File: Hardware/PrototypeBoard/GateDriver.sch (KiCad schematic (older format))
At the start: 38 parts, among them U4 TLE7185-1E

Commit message: more layout and some changes to schematic
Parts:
- TP10, TP11, TP12, TP13, TP14, TP15, TP16, TP17, TP18, TP19, TP20, TP21, TP6, TP7, TP8, TP9: footprint Measurement_Points:Measurement_Point_Round-SMD-Pad_Small -> Pin_Headers:Pin_Header_Straight_1x01_Pitch2.00mm
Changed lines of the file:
@@
 F 0 "TP17" H 6950 2900 50  0000 C BNN
 F 1 "BstV" H 6950 2850 50  0000 C CNN
-F 2 "Measurement_Points:Measurement_Point_Round-SMD-Pad_Small" H 6950 2600 50  0001 C CNN
+F 2 "Pin_Headers:Pin_Header_Straight_1x01_Pitch2.00mm" H 6950 2600 50  0001 C CNN
 F 3 "" H 6950 2600 50  0001 C CNN
 	1    6950 2600
@@
 F 0 "TP16" H 6950 2200 50  0000 C BNN
 F 1 "BstU" H 6950 2150 50  0000 C CNN
-F 2 "Measurement_Points:Measurement_Point_Round-SMD-Pad_Small" H 6950 1900 50  0001 C CNN
+F 2 "Pin_Headers:Pin_Header_Straight_1x01_Pitch2.00mm" H 6950 1900 50  0001 C CNN
 F 3 "" H 6950 1900 50  0001 C CNN
 	1    6950 1900
@@
 F 0 "TP18" H 6950 3600 50  0000 C BNN
 F 1 "BstW" H 6950 3550 50  0000 C CNN
-F 2 "Measurement_Points:Measurement_Point_Round-SMD-Pad_Small" H 6950 3300 50  0001 C CNN
+F 2 "Pin_Headers:Pin_Header_Straight_1x01_Pitch2.00mm" H 6950 3300 50  0001 C CNN
 F 3 "" H 6950 3300 50  0001 C CNN
 	1    6950 3300
@@
 F 0 "TP14" H 6200 3000 50  0000 C BNN
 F 1 "GateVH" H 6200 2950 50  0000 C CNN
-F 2 "Measurement_Points:Measurement_Point_Round-SMD-Pad_Small" H 6200 2700 50  0001 C CNN
+F 2 "Pin_Headers:Pin_Header_Straight_1x01_Pitch2.00mm" H 6200 2700 50  0001 C CNN
 F 3 "" H 6200 2700 50  0001 C CNN
 	1    6200 2700
@@
 F 0 "TP13" H 6200 2300 50  0000 C BNN
 F 1 "GateUH" H 6200 2250 50  0000 C CNN
-F 2 "Measurement_Points:Measurement_Point_Round-SMD-Pad_Small" H 6200 2000 50  0001 C CNN
+F 2 "Pin_Headers:Pin_Header_Straight_1x01_Pitch2.00mm" H 6200 2000 50  0001 C CNN
 F 3 "" H 6200 2000 50  0001 C CNN
 	1    6200 2000
@@
 F 0 "TP15" H 6200 3700 50  0000 C BNN
 F 1 "GateWH" H 6200 3650 50  0000 C CNN
-F 2 "Measurement_Points:Measurement_Point_Round-SMD-Pad_Small" H 6200 3400 50  0001 C CNN
+F 2 "Pin_Headers:Pin_Header_Straight_1x01_Pitch2.00mm" H 6200 3400 50  0001 C CNN
 F 3 "" H 6200 3400 50  0001 C CNN
 	1    6200 3400
@@
 F 0 "TP19" H 6950 4300 50  0000 C BNN
 F 1 "GateUL" H 6950 4250 50  0000 C CNN
-F 2 "Measurement_Points:Measurement_Point_Round-SMD-Pad_Small" H 6950 4000 50  0001 C CNN
+F 2 "Pin_Headers:Pin_Header_Straight_1x01_Pitch2.00mm" H 6950 4000 50  0001 C CNN
 F 3 "" H 6950 4000 50  0001 C CNN
 	1    6950 4000
@@
 F 0 "TP20" H 6950 4800 50  0000 C BNN
 F 1 "GateVL" H 6950 4750 50  0000 C CNN
-F 2 "Measurement_Points:Measurement_Point_Round-SMD-Pad_Small" H 6950 4500 50  0001 C CNN
+F 2 "Pin_Headers:Pin_Header_Straight_1x01_Pitch2.00mm" H 6950 4500 50  0001 C CNN
 F 3 "" H 6950 4500 50  0001 C CNN
 	1    6950 4500
@@
 F 0 "TP21" H 6950 5300 50  0000 C BNN
 F 1 "GateWL" H 6950 5250 50  0000 C CNN
-F 2 "Measurement_Points:Measurement_Point_Round-SMD-Pad_Small" H 6950 5000 50  0001 C CNN
+F 2 "Pin_Headers:Pin_Header_Straight_1x01_Pitch2.00mm" H 6950 5000 50  0001 C CNN
 F 3 "" H 6950 5000 50  0001 C CNN
 	1    6950 5000
@@
 F 0 "TP9" H 1900 3400 50  0000 C BNN
 F 1 "GdEna" H 1900 3350 50  0000 C CNN
-F 2 "Measurement_Points:Measurement_Point_Round-SMD-Pad_Small" H 1900 3100 50  0001 C CNN
+F 2 "Pin_Headers:Pin_Header_Straight_1x01_Pitch2.00mm" H 1900 3100 50  0001 C CNN
 F 3 "" H 1900 3100 50  0001 C CNN
 	1    1900 3100
@@
 F 0 "TP10" H 1900 3700 50  0000 C BNN
 F 1 "PwmUL" H 1900 3650 50  0000 C CNN
-F 2 "Measurement_Points:Measurement_Point_Round-SMD-Pad_Small" H 1900 3400 50  0001 C CNN
+F 2 "Pin_Headers:Pin_Header_Straight_1x01_Pitch2.00mm" H 1900 3400 50  0001 C CNN
 F 3 "" H 1900 3400 50  0001 C CNN
 	1    1900 3400
@@
 F 0 "TP6" H 1700 3900 50  0000 C BNN
 F 1 "~PwmUH" H 1700 3850 50  0000 C CNN
-F 2 "Measurement_Points:Measurement_Point_Round-SMD-Pad_Small" H 1700 3600 50  0001 C CNN
+F 2 "Pin_Headers:Pin_Header_Straight_1x01_Pitch2.00mm" H 1700 3600 50  0001 C CNN
 F 3 "" H 1700 3600 50  0001 C CNN
 	1    1700 3600
@@
 F 0 "TP11" H 1900 4200 50  0000 C BNN
 F 1 "PwmVL" H 1900 4150 50  0000 C CNN
-F 2 "Measurement_Points:Measurement_Point_Round-SMD-Pad_Small" H 1900 3900 50  0001 C CNN
+F 2 "Pin_Headers:Pin_Header_Straight_1x01_Pitch2.00mm" H 1900 3900 50  0001 C CNN
 F 3 "" H 1900 3900 50  0001 C CNN
 	1    1900 3900
@@
 F 0 "TP7" H 1700 4400 50  0000 C BNN
 F 1 "~PwmVH" H 1700 4350 50  0000 C CNN
-F 2 "Measurement_Points:Measurement_Point_Round-SMD-Pad_Small" H 1700 4100 50  0001 C CNN
+F 2 "Pin_Headers:Pin_Header_Straight_1x01_Pitch2.00mm" H 1700 4100 50  0001 C CNN
 F 3 "" H 1700 4100 50  0001 C CNN
 	1    1700 4100
@@
 F 0 "TP12" H 1900 4700 50  0000 C BNN
 F 1 "PwmWL" H 1900 4650 50  0000 C CNN
-F 2 "Measurement_Points:Measurement_Point_Round-SMD-Pad_Small" H 1900 4400 50  0001 C CNN
+F 2 "Pin_Headers:Pin_Header_Straight_1x01_Pitch2.00mm" H 1900 4400 50  0001 C CNN
 F 3 "" H 1900 4400 50  0001 C CNN
 	1    1900 4400
@@
 F 0 "TP8" H 1700 4900 50  0000 C BNN
 F 1 "~PwmWH" H 1700 4850 50  0000 C CNN
-F 2 "Measurement_Points:Measurement_Point_Round-SMD-Pad_Small" H 1700 4600 50  0001 C CNN
+F 2 "Pin_Headers:Pin_Header_Straight_1x01_Pitch2.00mm" H 1700 4600 50  0001 C CNN
 F 3 "" H 1700 4600 50  0001 C CNN
 	1    1700 4600

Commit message: Migrated to kicad 5
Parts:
- C21, C22, C23, C24, C25, C26: symbol C -> Device:C
- R11, R12, R13, R14, R15, R16, R17, R18, R19, R20, R21, R22, R23, R24, R25: symbol R -> Device:R
- TP10, TP11, TP12, TP13, TP14, TP15, TP16, TP17, TP18, TP19, TP20, TP21, TP6, TP7, TP8, TP9: symbol TEST -> PrototypeBoard-rescue:TEST
- U4: symbol TLE7185-1E -> PrototypeBoard-rescue:TLE7185-1E
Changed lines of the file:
@@
-EESchema Schematic File Version 2
-LIBS:power
-LIBS:device
-LIBS:switches
-LIBS:relays
-LIBS:motors
-LIBS:transistors
-LIBS:conn
-LIBS:linear
-LIBS:regul
-LIBS:74xx
-LIBS:cmos4000
-LIBS:adc-dac
-LIBS:memory
-LIBS:xilinx
-LIBS:microcontrollers
-LIBS:dsp
-LIBS:microchip
-LIBS:analog_switches
-LIBS:motorola
-LIBS:texas
-LIBS:intel
-LIBS:audio
-LIBS:interface
-LIBS:digital-audio
-LIBS:philips
-LIBS:display
-LIBS:cypress
-LIBS:siliconi
-LIBS:opto
-LIBS:atmel
-LIBS:contrib
-LIBS:valves
+EESchema Schematic File Version 4
 LIBS:PrototypeBoard-cache
-EELAYER 25 0
+EELAYER 26 0
 EELAYER END
 $Descr A4 11693 8268
@@
 $EndDescr
 $Comp
-L TLE7185-1E U4
+L PrototypeBoard-rescue:TLE7185-1E U4
 U 1 1 56C10CBD
 P 4500 3600
@@
 Logic_GD_ENA
 $Comp
-L R R14
+L Device:R R14
 U 1 1 56C25790
 P 3050 2800
@@
 $EndComp
 $Comp
-L R R13
+L Device:R R13
 U 1 1 56C257FB
 P 3050 2600
@@
 ~Logic_GD_ERR2
 $Comp
-L C C22
+L Device:C C22
 U 1 1 56C25879
 P 2950 2200
@@
 	3150 2350 2950 2350
 $Comp
-L C C21
+L Device:C C21
 U 1 1 56C25915
 P 2600 2050
@@
 	2600 1900 3300 1900
 $Comp
-L GND #PWR032
+L power:GND #PWR032
 U 1 1 56C259AC
 P 2600 2200
@@
 $EndComp
 $Comp
-L R R11
+L Device:R R11
 U 1 1 56C25A1A
 P 1800 4950
@@
 $EndComp
 $Comp
-L R R12
+L Device:R R12
 U 1 1 56C25AD5
 P 1800 5250
@@
 $EndComp
 $Comp
-L R R15
+L Device:R R15
 U 1 1 56C25B0C
 P 3100 5450
@@
 	3300 5300 3100 5300
 $Comp
-L GND #PWR033
+L power:GND #PWR033
 U 1 1 56C25C22
 P 1800 5400
@@
 $EndComp
 $Comp
-L GND #PWR034
+L power:GND #PWR034
 U 1 1 56C25CA5
 P 3100 5600
@@
 $EndComp
 $Comp
-L +3.3V #PWR035
+L power:+3.3V #PWR035
 U 1 1 56C25D62
 P 1800 4800
@@
 $EndComp
 $Comp
-L R R18
+L Device:R R18
 U 1 1 56C25E1E
 P 4500 1050
@@
 $EndComp
 $Comp
-L C C23
+L Device:C C23
 U 1 1 56C25EA2
 P 4700 1450
@@
 $EndComp
 $Comp
-L GND #PWR036
+L power:GND #PWR036
 U 1 1 56C2602E
 P 4700 1600
@@
 $EndComp
 $Comp
-L +BATT #PWR037
+L power:+BATT #PWR037
 U 1 1 56C261FD
 P 4500 800
@@
 $EndComp
 $Comp
-L R R19
+L Device:R R19
 U 1 1 56C26356
 P 4950 1350
@@
 	4950 1500 4950 1600
 $Comp
-L +BATT #PWR038
+L power:+BATT #PWR038
 U 1 1 56C26408
 P 4950 1200
@@
 Source_W_H
 $Comp
-L C C24
+L Device:C C24
 U 1 1 56C26607
 P 6950 2100
@@
 $EndComp
 $Comp
-L C C25
+L Device:C C25
 U 1 1 56C266D2
 P 6950 2800
@@
 $EndComp
 $Comp
-L C C26
+L Device:C C26
 U 1 1 56C26727
 P 6950 3500
@@
 Gate_W_L
 $Comp
-L R R25
+L Device:R R25
 U 1 1 56C2703F
 P 5950 5100
@@
 $EndComp
 $Comp
-L R R24
+L Device:R R24
 U 1 1 56C271C9
 P 5950 4600
@@
 Gate_U_L
 $Comp
-L R R23
+L Device:R R23
 U 1 1 56C27221
 P 5950 4100
@@
 $EndComp
 $Comp
-L R R22
+L Device:R R22
 U 1 1 56C2752F
 P 5950 3500
@@
 $EndComp
 $Comp
-L R R21
+L Device:R R21
 U 1 1 56C2759F
 P 5950 2800
@@
 $EndComp
 $Comp
-L R R20
+L Device:R R20
 U 1 1 56C27617
 P 5950 2100
@@
 $EndComp
 $Comp
-L GND #PWR039
+L power:GND #PWR039
 U 1 1 56C35C82
 P 4050 5600
@@
 $EndComp
 $Comp
-L GND #PWR040
+L power:GND #PWR040
 U 1 1 56C35CC9
 P 4350 5600
@@
 $EndComp
 $Comp
-L GND #PWR041
+L power:GND #PWR041
 U 1 1 56C35D10
 P 4650 5600
@@
 $EndComp
 $Comp
-L GND #PWR042
+L power:GND #PWR042
 U 1 1 56C35D57
 P 4950 5600
@@
 $EndComp
 $Comp
-L R R16
+L Device:R R16
 U 1 1 56C36A2B
 P 3850 1450
@@
 $EndComp
 $Comp
-L GND #PWR043
+L power:GND #PWR043
 U 1 1 56C36B52
 P 3850 1600
@@
 $EndComp
 $Comp
-L R R17
+L Device:R R17
 U 1 1 56C36CC4
 P 4050 1050
@@
 $EndComp
 $Comp
-L +BATT #PWR044
+L power:+BATT #PWR044
 U 1 1 56C36FE8
 P 4050 800
@@
 Gate_U_H
 $Comp
-L GND #PWR045
+L power:GND #PWR045
 U 1 1 5AFC4218
 P 3250 3000
@@
 	2800 4700 3300 4700
 $Comp
-L TEST TP17
+L PrototypeBoard-rescue:TEST TP17
 U 1 1 5B00632C
 P 6950 2600
@@
 $EndComp
 $Comp
-L TEST TP16
+L PrototypeBoard-rescue:TEST TP16
 U 1 1 5B00675F
 P 6950 1900
@@
 $EndComp
 $Comp
-L TEST TP18
+L PrototypeBoard-rescue:TEST TP18
 U 1 1 5B0067D7
 P 6950 3300
@@
 $EndComp
 $Comp
-L TEST TP14
+L PrototypeBoard-rescue:TEST TP14
 U 1 1 5B006F17
 P 6200 2700
@@
 $EndComp
 $Comp
-L TEST TP13
+L PrototypeBoard-rescue:TEST TP13
 U 1 1 5B007003
 P 6200 2000
@@
 $EndComp
 $Comp
-L TEST TP15
+L PrototypeBoard-rescue:TEST TP15
 U 1 1 5B00714B
 P 6200 3400
@@
 $EndComp
 $Comp
-L TEST TP19
+L PrototypeBoard-rescue:TEST TP19
 U 1 1 5B007271
 P 6950 4000
@@
 $EndComp
 $Comp
-L TEST TP20
+L PrototypeBoard-rescue:TEST TP20
 U 1 1 5B0073EE
 P 6950 4500
@@
 $EndComp
 $Comp
-L TEST TP21
+L PrototypeBoard-rescue:TEST TP21
 U 1 1 5B007541
 P 6950 5000
@@
 Connection ~ 7200 2300
 $Comp
-L TEST TP9
+L PrototypeBoard-rescue:TEST TP9
 U 1 1 5B007A76
 P 1900 3100
@@
 $EndComp
 $Comp
-L TEST TP10
+L PrototypeBoard-rescue:TEST TP10
 U 1 1 5B007E0F
 P 1900 3400
@@
 $EndComp
 $Comp
-L TEST TP6
+L PrototypeBoard-rescue:TEST TP6
 U 1 1 5B007F38
 P 1700 3600
@@
 $EndComp
 $Comp
-L TEST TP11
+L PrototypeBoard-rescue:TEST TP11
 U 1 1 5B007FCC
 P 1900 3900
@@
 $EndComp
 $Comp
-L TEST TP7
+L PrototypeBoard-rescue:TEST TP7
 U 1 1 5B008063
 P 1700 4100
@@
 $EndComp
 $Comp
-L TEST TP12
+L PrototypeBoard-rescue:TEST TP12
 U 1 1 5B0080F9
 P 1900 4400
@@
 $EndComp
 $Comp
-L TEST TP8
+L PrototypeBoard-rescue:TEST TP8
 U 1 1 5B008196
 P 1700 4600
@@
 Connection ~ 4500 1300
 $Comp
-L PWR_FLAG #FLG046
+L power:PWR_FLAG #FLG046
 U 1 1 5AFF78D6
 P 4300 1000

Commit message: Layout almost done
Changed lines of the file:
@@
 $EndComp
 Wire Wire Line
-	5700 2300 7300 2300
+	5700 2300 6950 2300
 Wire Wire Line
 	6950 2250 6950 2300
 Connection ~ 6950 2300
 Wire Wire Line
-	5700 3000 7300 3000
+	5700 3000 6950 3000
 Wire Wire Line
 	6950 2950 6950 3000
 Connection ~ 6950 3000
 Wire Wire Line
-	5700 3700 7300 3700
+	5700 3700 6950 3700
 Wire Wire Line
 	6950 3650 6950 3700
@@
 $EndComp
 Wire Wire Line
-	4050 1200 4050 1600
+	4050 1200 4050 1300
 Wire Wire Line
 	3850 1300 4050 1300
@@
 	5700 2100 5800 2100
 Wire Wire Line
-	6100 2100 6300 2100
+	6100 2100 6200 2100
 Wire Wire Line
 	5700 2800 5800 2800
 Wire Wire Line
-	6100 2800 6300 2800
+	6100 2800 6200 2800
 Wire Wire Line
 	5700 3500 5800 3500
 Wire Wire Line
-	6100 3500 6300 3500
+	6100 3500 6200 3500
 Wire Wire Line
 	5700 4100 5800 4100
 Wire Wire Line
-	6100 4100 6300 4100
+	6100 4100 6200 4100
 Wire Wire Line
 	5700 4300 6300 4300
@@
 	5700 4600 5800 4600
 Wire Wire Line
-	6100 4600 6300 4600
+	6100 4600 6200 4600
 Wire Wire Line
 	5700 4800 6300 4800
@@
 	5700 5100 5800 5100
 Wire Wire Line
-	6100 5100 6300 5100
+	6100 5100 6200 5100
 Wire Wire Line
 	5700 5300 6300 5300
 Wire Wire Line
-	2800 3200 3300 3200
-Wire Wire Line
-	2800 3500 3300 3500
-Wire Wire Line
-	2800 3700 3300 3700
-Wire Wire Line
-	2800 4000 3300 4000
-Wire Wire Line
-	2800 4200 3300 4200
-Wire Wire Line
-	2800 4500 3300 4500
-Wire Wire Line
-	2800 4700 3300 4700
+	2800 3200 2850 3200
+Wire Wire Line
+	2800 3500 2850 3500
+Wire Wire Line
+	2800 3700 2850 3700
+Wire Wire Line
+	2800 4000 2850 4000
+Wire Wire Line
+	2800 4200 2850 4200
+Wire Wire Line
+	2800 4500 2850 4500
+Wire Wire Line
+	2800 4700 2850 4700
 $Comp
 L PrototypeBoard-rescue:TEST TP17
@@
 	0    1    1    0
 $EndComp
-Connection ~ 7200 3700
-Connection ~ 7200 3000
-Connection ~ 7200 2300
 $Comp
 L PrototypeBoard-rescue:TEST TP9
@@
 	4500 800  4500 900
 Wire Wire Line
-	4500 1200 4500 1600
-Wire Wire Line
-	4300 1300 4700 1300
+	4500 1200 4500 1300
+Wire Wire Line
+	4300 1300 4500 1300
 Connection ~ 4500 1300
 $Comp
@@
 Text Label 5750 5100 0    60   ~ 0
 Gate_W_L_bR
+Wire Wire Line
+	2850 3200 3300 3200
+Wire Wire Line
+	2850 3500 3300 3500
+Wire Wire Line
+	2850 3700 3300 3700
+Wire Wire Line
+	2850 4000 3300 4000
+Wire Wire Line
+	2850 4200 3300 4200
+Wire Wire Line
+	2850 4500 3300 4500
+Wire Wire Line
+	2850 4700 3300 4700
+Wire Wire Line
+	4050 1300 4050 1600
+Wire Wire Line
+	6200 2100 6300 2100
+Wire Wire Line
+	6200 2800 6300 2800
+Wire Wire Line
+	6200 3500 6300 3500
+Wire Wire Line
+	6200 4100 6300 4100
+Wire Wire Line
+	6200 5100 6300 5100
+Wire Wire Line
+	6200 4600 6300 4600
+Wire Wire Line
+	4500 1300 4500 1600
+Wire Wire Line
+	4500 1300 4700 1300
+Wire Wire Line
+	6950 2300 7300 2300
+Wire Wire Line
+	6950 3000 7300 3000
+Wire Wire Line
+	6950 3700 7300 3700
 $EndSCHEMATC

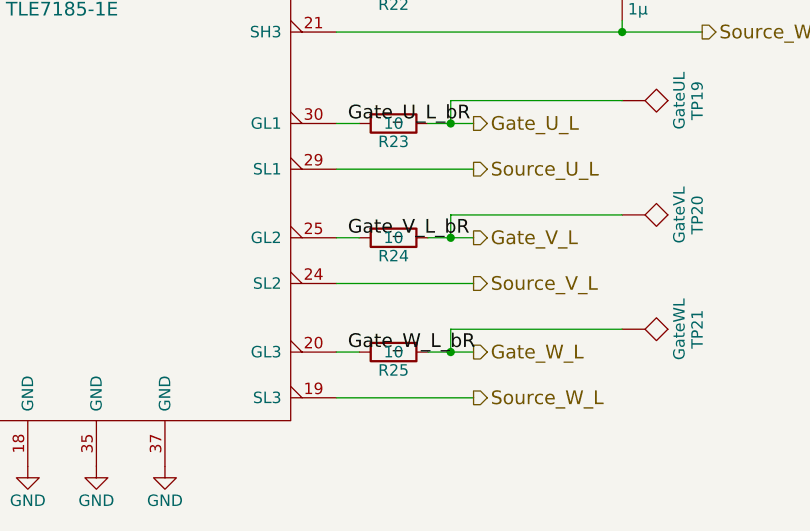
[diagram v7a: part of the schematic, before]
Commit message: New, much bigger pcb layout, changes to connection PGND <-> GND
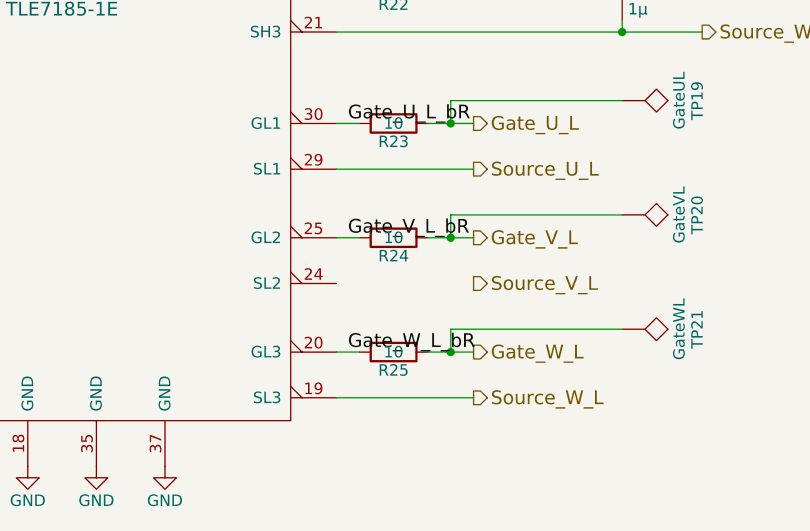
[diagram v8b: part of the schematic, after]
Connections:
- net Source_V_L: no longer U4.24 (SL2)
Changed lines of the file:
@@
 	2600 1900 3300 1900
 $Comp
-L power:GND #PWR032
+L power:GND #PWR038
 U 1 1 56C259AC
 P 2600 2200
-F 0 "#PWR032" H 2600 1950 50  0001 C CNN
+F 0 "#PWR038" H 2600 1950 50  0001 C CNN
 F 1 "GND" H 2600 2050 50  0000 C CNN
 F 2 "" H 2600 2200 50  0000 C CNN
@@
 	3300 5300 3100 5300
 $Comp
-L power:GND #PWR033
+L power:GND #PWR037
 U 1 1 56C25C22
 P 1800 5400
-F 0 "#PWR033" H 1800 5150 50  0001 C CNN
+F 0 "#PWR037" H 1800 5150 50  0001 C CNN
 F 1 "GND" H 1800 5250 50  0000 C CNN
 F 2 "" H 1800 5400 50  0000 C CNN
@@
 $EndComp
 $Comp
-L power:GND #PWR034
+L power:GND #PWR039
 U 1 1 56C25CA5
 P 3100 5600
-F 0 "#PWR034" H 3100 5350 50  0001 C CNN
+F 0 "#PWR039" H 3100 5350 50  0001 C CNN
 F 1 "GND" H 3100 5450 50  0000 C CNN
 F 2 "" H 3100 5600 50  0000 C CNN
@@
 $EndComp
 $Comp
-L power:+3.3V #PWR035
+L power:+3.3V #PWR036
 U 1 1 56C25D62
 P 1800 4800
-F 0 "#PWR035" H 1800 4650 50  0001 C CNN
+F 0 "#PWR036" H 1800 4650 50  0001 C CNN
 F 1 "+3.3V" H 1800 4940 50  0000 C CNN
 F 2 "" H 1800 4800 50  0000 C CNN
@@
 $EndComp
 $Comp
-L power:GND #PWR036
+L power:GND #PWR047
 U 1 1 56C2602E
 P 4700 1600
-F 0 "#PWR036" H 4700 1350 50  0001 C CNN
+F 0 "#PWR047" H 4700 1350 50  0001 C CNN
 F 1 "GND" H 4700 1450 50  0000 C CNN
 F 2 "" H 4700 1600 50  0000 C CNN
@@
 $EndComp
 $Comp
-L power:+BATT #PWR037
+L power:+BATT #PWR045
 U 1 1 56C261FD
 P 4500 800
-F 0 "#PWR037" H 4500 650 50  0001 C CNN
+F 0 "#PWR045" H 4500 650 50  0001 C CNN
 F 1 "+BATT" H 4500 940 50  0000 C CNN
 F 2 "" H 4500 800 50  0000 C CNN
@@
 	4950 1500 4950 1600
 $Comp
-L power:+BATT #PWR038
+L power:+BATT #PWR048
 U 1 1 56C26408
 P 4950 1200
-F 0 "#PWR038" H 4950 1050 50  0001 C CNN
+F 0 "#PWR048" H 4950 1050 50  0001 C CNN
 F 1 "+BATT" H 4950 1340 50  0000 C CNN
 F 2 "" H 4950 1200 50  0000 C CNN
@@
 $EndComp
 $Comp
-L power:GND #PWR039
+L power:GND #PWR043
 U 1 1 56C35C82
 P 4050 5600
-F 0 "#PWR039" H 4050 5350 50  0001 C CNN
+F 0 "#PWR043" H 4050 5350 50  0001 C CNN
 F 1 "GND" H 4050 5450 50  0000 C CNN
 F 2 "" H 4050 5600 50  0000 C CNN
@@
 $EndComp
 $Comp
-L power:GND #PWR040
+L power:GND #PWR044
 U 1 1 56C35CC9
 P 4350 5600
-F 0 "#PWR040" H 4350 5350 50  0001 C CNN
+F 0 "#PWR044" H 4350 5350 50  0001 C CNN
 F 1 "GND" H 4350 5450 50  0000 C CNN
 F 2 "" H 4350 5600 50  0000 C CNN
@@
 $EndComp
 $Comp
-L power:GND #PWR041
+L power:GND #PWR046
 U 1 1 56C35D10
 P 4650 5600
-F 0 "#PWR041" H 4650 5350 50  0001 C CNN
+F 0 "#PWR046" H 4650 5350 50  0001 C CNN
 F 1 "GND" H 4650 5450 50  0000 C CNN
 F 2 "" H 4650 5600 50  0000 C CNN
@@
 $EndComp
 $Comp
-L power:GND #PWR042
+L power:GND #PWR049
 U 1 1 56C35D57
 P 4950 5600
-F 0 "#PWR042" H 4950 5350 50  0001 C CNN
+F 0 "#PWR049" H 4950 5350 50  0001 C CNN
 F 1 "GND" H 4950 5450 50  0000 C CNN
 F 2 "" H 4950 5600 50  0000 C CNN
@@
 $EndComp
 $Comp
-L power:GND #PWR043
+L power:GND #PWR041
 U 1 1 56C36B52
 P 3850 1600
-F 0 "#PWR043" H 3850 1350 50  0001 C CNN
+F 0 "#PWR041" H 3850 1350 50  0001 C CNN
 F 1 "GND" H 3850 1450 50  0000 C CNN
 F 2 "" H 3850 1600 50  0000 C CNN
@@
 $EndComp
 $Comp
-L power:+BATT #PWR044
+L power:+BATT #PWR042
 U 1 1 56C36FE8
 P 4050 800
-F 0 "#PWR044" H 4050 650 50  0001 C CNN
+F 0 "#PWR042" H 4050 650 50  0001 C CNN
 F 1 "+BATT" H 4050 940 50  0000 C CNN
 F 2 "" H 4050 800 50  0000 C CNN
@@
 Gate_U_H
 $Comp
-L power:GND #PWR045
+L power:GND #PWR040
 U 1 1 5AFC4218
 P 3250 3000
-F 0 "#PWR045" H 3250 2750 50  0001 C CNN
+F 0 "#PWR040" H 3250 2750 50  0001 C CNN
 F 1 "GND" H 3250 2850 50  0000 C CNN
 F 2 "" H 3250 3000 50  0000 C CNN
@@
 Wire Wire Line
 	6100 4600 6200 4600
-Wire Wire Line
-	5700 4800 6300 4800
 Wire Wire Line
 	5700 5100 5800 5100
@@
 Connection ~ 4500 1300
 $Comp
-L power:PWR_FLAG #FLG046
+L power:PWR_FLAG #FLG01
 U 1 1 5AFF78D6
 P 4300 1000
-F 0 "#FLG046" H 4300 1075 50  0001 C CNN
+F 0 "#FLG01" H 4300 1075 50  0001 C CNN
 F 1 "PWR_FLAG" H 4300 1150 50  0000 C CNN
 F 2 "" H 4300 1000 50  0001 C CNN
